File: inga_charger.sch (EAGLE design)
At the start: 10 parts

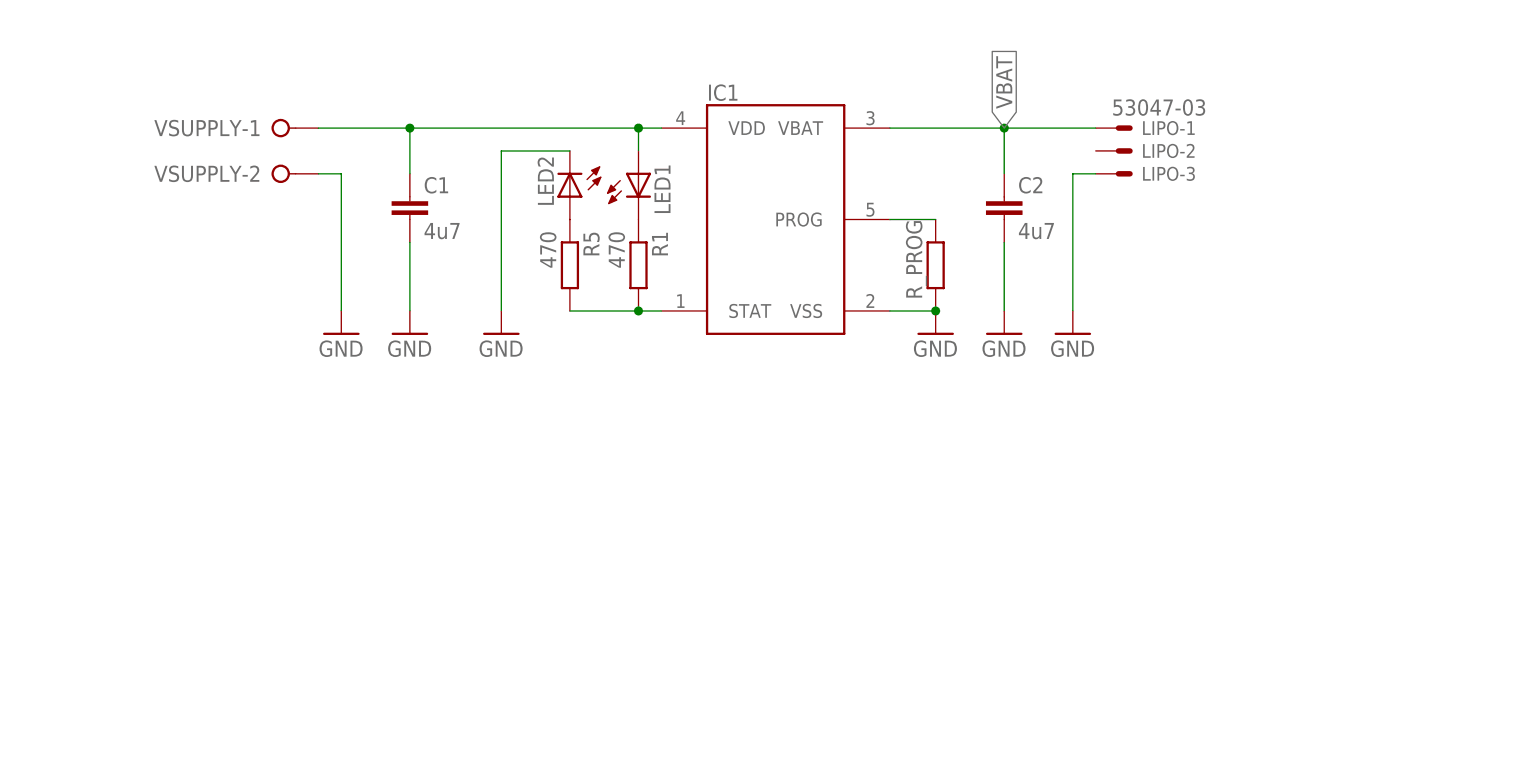
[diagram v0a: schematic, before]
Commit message: Adds new version of board and schematic
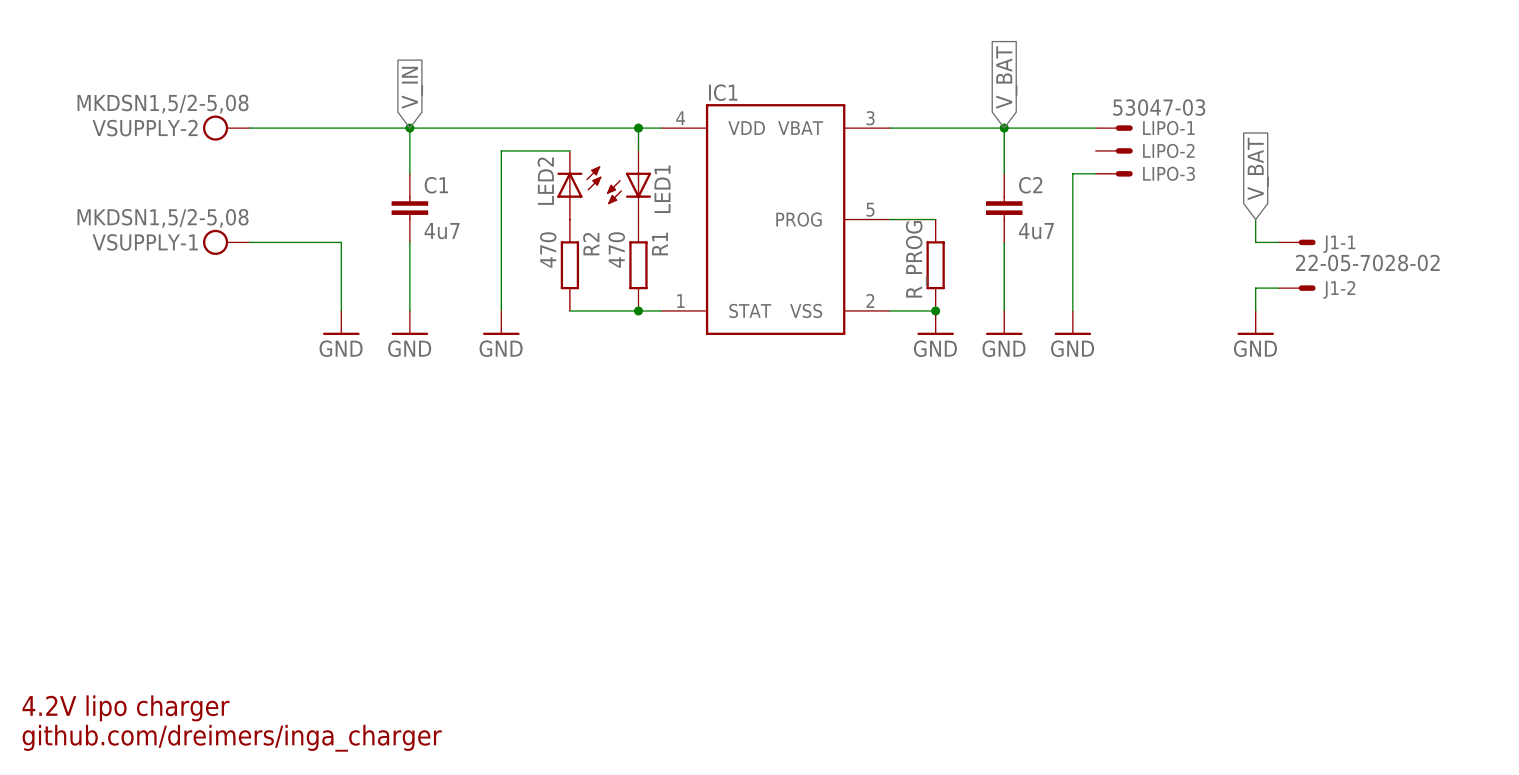
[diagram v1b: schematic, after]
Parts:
- added J1: 22-05-7028-02, con-molex:22-05-7028-02
- VSUPPLY: value (none) -> MKDSN1,5/2-5,08; device con-wago-508:W237-02P -> con-phoenix-508:MKDSN1,5/2-5,08
- renumbered R5 to R2
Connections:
- removed net VBAT: C2.1, IC1.VBAT, LIPO-1.S
- removed net VDD: C1.1, IC1.VDD, LED1.A, VSUPPLY-1.KL
- new net V_BAT: C2.1, IC1.VBAT, J1-1.S, LIPO-1.S
- new net V_IN: C1.1, IC1.VDD, LED1.A, VSUPPLY-2.KL
- net GND: now also J1-2.S, VSUPPLY-1.KL; no longer VSUPPLY-2.KL
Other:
- note added: "4.2V lipo charger github.com/dreimers/inga_charger"
